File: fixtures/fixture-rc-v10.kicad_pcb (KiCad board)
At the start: 2 copper layers, 30 x 20 mm, 2 parts

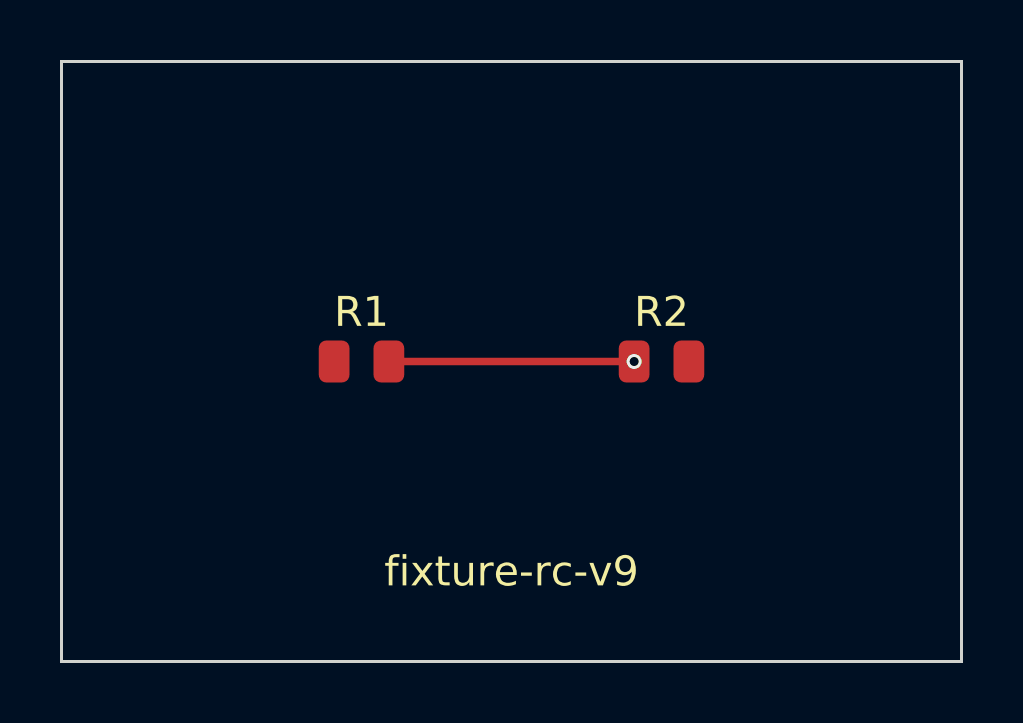
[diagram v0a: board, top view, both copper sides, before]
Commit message: docs: reposition around any routed KiCad board, one fidelity source, KiCad 6 to 10 statement (fixes #64, fixes #65, fixes #61, fixes #63)
- README and site: lead with simulate and audit any routed KiCad board; Quilter is one named way in, the schematic is an optional input picked up next to the board; state that the simulation treats nets as ideal nodes and the Critic reads the copper.
- Fidelity: website/docs/concepts/fidelity.md is the only source. scripts/fidelity-doc.mjs renders it to docs/what-circsim-can-tell-you.html, which the app opens instead of raw markdown. The old markdown copy is deleted; a test fails on drift.
- KiCad support: README and docs say KiCad 6 to 10 with a version table derived row for row from scripts/corpus-manifest.json, the rejected RoyalBlue54L-Feather board named. Name-only nets are attributed to KiCad 10 (format 20260206); fixture-rc-v9 renamed fixture-rc-v10.

Co-Authored-By: Claude Sonnet 5.5 <noreply@anthropic.com>
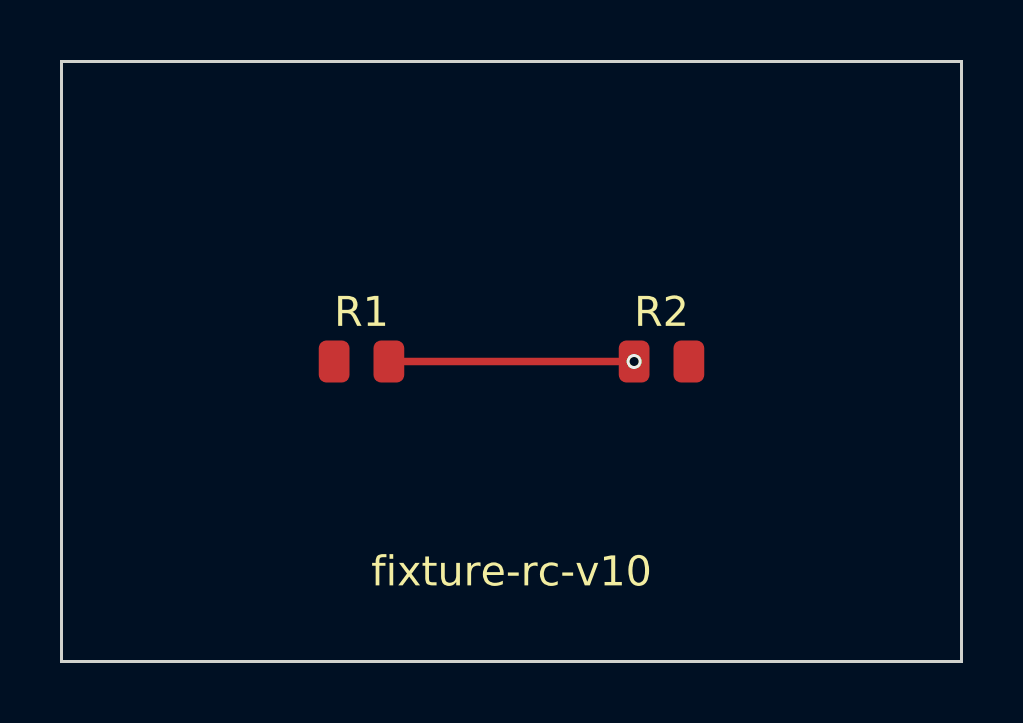
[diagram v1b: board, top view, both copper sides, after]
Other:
- board text added: "fixture-rc-v10"
- board text removed: "fixture-rc-v9"
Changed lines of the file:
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@@
   (via (at 19.0875 10) (size 0.5) (drill 0.3) (layers "F.Cu" "B.Cu")
     (net "OUT"))
-  (gr_text "fixture-rc-v9" (at 15 17) (layer "F.SilkS")
+  (gr_text "fixture-rc-v10" (at 15 17) (layer "F.SilkS")
     (effects (font (size 1 1) (thickness 0.15))))
   (gr_line (start 0 0) (end 30 0) (layer "Edge.Cuts") (width 0.1))
